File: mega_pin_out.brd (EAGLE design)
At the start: 100 x 80 mm, 11 parts, among them X1 332-36

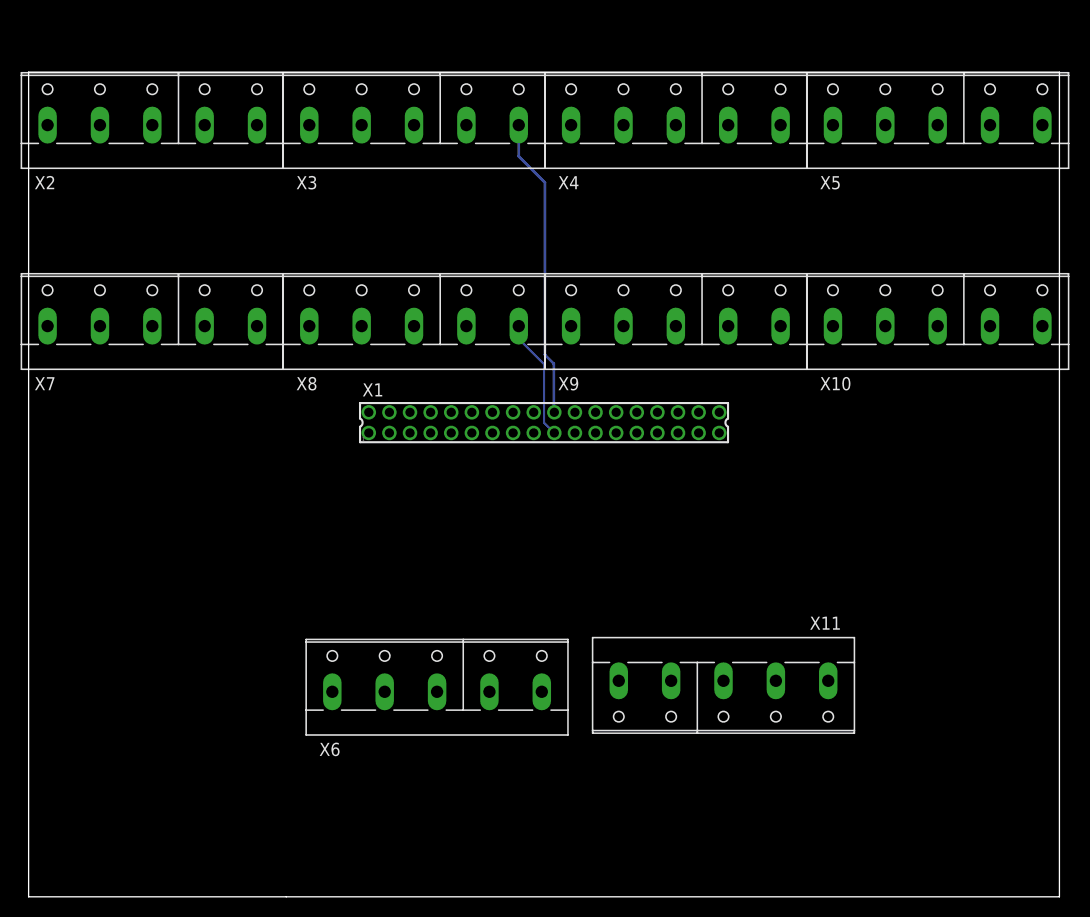
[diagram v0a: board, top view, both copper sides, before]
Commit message: Full reroute of 2x18 female pins
- Fixed the female pins pcb layout part size
- Reroute all pins
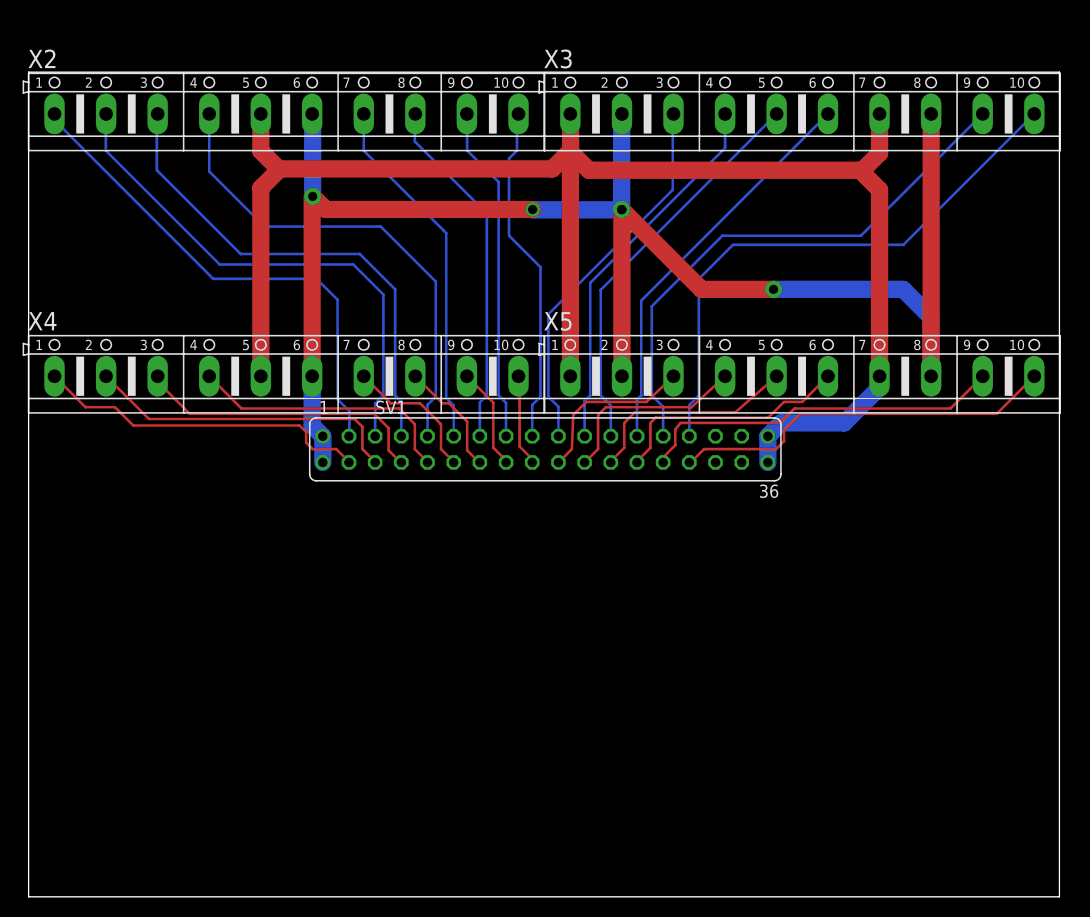
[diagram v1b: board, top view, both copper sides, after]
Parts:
- removed X1: 332-36, con-garry:332-36
- removed X10, X11, X6, X7, X8, X9: (no value), con-wago-508:W237-5P
- added SV1: (no value), con-lsta:FE18-2
- X2, X3, X4, X5: device con-wago-508:W237-5P -> con-ptr500:AK500/10
- moved X4 45.3 mm to (25.0, 50.5)
- moved X3 37.7 mm to (75.1, 75.9)
- moved X5 28.2 mm to (75.1, 50.5)
- moved X2 13.0 mm to (25.0, 75.9)
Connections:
- removed net I22: X1.3
- removed net I23: X1.4
- removed net I24: X1.5
- removed net I25: X1.6
- removed net I26: X1.7
- removed net I27: X1.8
- removed net I28: X1.9
- removed net I29: X1.10
- removed net I30: X1.11
- removed net I32: X1.13
- removed net I34: X1.15
- removed net I36: X1.17
- removed net I37: X1.18
- removed net I38: X1.19, X8.5
- removed net I39: X1.20, X3.5
- removed net N$1: X3.1
- removed net N$2: X3.2
- removed net N$30: X1.24
- removed net N$31: X1.26
- removed net N$32: X1.28
- removed net N$33: X1.30
- removed net N$34: X1.32
- removed net N$35: X1.34
- removed net N$36: X1.36
- removed net N$37: X6.1
- removed net N$38: X6.2
- removed net N$39: X6.3
- removed net N$40: X6.4
- removed net N$41: X6.5
- removed net N$42: X8.4
- removed net N$43: X8.3
- removed net N$6: X2.1
- removed net N$7: X2.2
- removed net N$8: X2.3
- new net GND: SV1.35, SV1.36, X2.5, X3.1, X3.7, X4.5, X5.1, X5.7
- new net I47: SV1.27, X3.9
- new net I49: SV1.29, X3.10
- net 5V: now also SV1.1, SV1.2, X2.6, X3.2, X3.8, X4.6, X5.2, X5.8; no longer X1.1, X1.2
- net I31: now also SV1.11, X2.7; no longer X1.12
- net I33: now also SV1.13, X2.8; no longer X1.14
- net I35: now also SV1.15, X2.9; no longer X1.16
- net N$10: now also SV1.9, X2.4; no longer X2.5
- net N$11: now also SV1.17, X2.10; no longer X1.21
- net N$12: now also SV1.19, X3.3; no longer X1.23
- net N$13: now also SV1.21, X3.4; no longer X1.25
- net N$14: now also SV1.23, X3.5; no longer X1.27
- net N$15: now also SV1.25, X3.6; no longer X1.29
- net N$16: now also SV1.4, X4.1; no longer X1.31
- net N$17: now also SV1.6, X4.2; no longer X1.33
- net N$18: now also SV1.8, X4.3; no longer X1.35
- net N$19: now also SV1.10, X4.4; no longer X4.1
- net N$20: now also SV1.12, X4.7; no longer X4.2
- net N$21: now also SV1.14, X4.8; no longer X4.3
- net N$22: now also SV1.16, X4.9; no longer X4.4
- net N$23: now also SV1.18, X4.10; no longer X4.5
- net N$24: now also SV1.20, X5.3; no longer X5.1
- net N$25: now also SV1.22, X5.4; no longer X5.2
- net N$26: now also SV1.24, X5.5; no longer X5.3
- net N$27: now also SV1.26, X5.6; no longer X5.4
- net N$28: now also SV1.28, X5.9; no longer X5.5
- net N$29: now also SV1.30, X5.10; no longer X1.22
- net N$3: now also SV1.3, X2.1; no longer X3.3
- net N$4: now also SV1.5, X2.2; no longer X3.4
- net N$9: now also SV1.7, X2.3; no longer X2.4
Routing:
- net GND: track 0.00 -> 157.4 mm
- net 5V: track 0.00 -> 155.8 mm, vias 0 -> 5
- net I49: track 0.00 -> 54.8 mm
- net I47: track 0.00 -> 52.9 mm
- net N$4: track 0.00 -> 50.3 mm
- net N$3: track 0.00 -> 49.0 mm
- net N$9: track 0.00 -> 47.9 mm
- net N$10: track 0.00 -> 47.3 mm
- net N$15: track 0.00 -> 38.9 mm
- net N$14: track 0.00 -> 38.7 mm
- net N$29: track 0.00 -> 37.5 mm
- net N$13: track 0.00 -> 37.0 mm
- net N$12: track 0.00 -> 36.7 mm
- net N$28: track 0.00 -> 35.7 mm
- net I31: track 0.00 -> 34.9 mm
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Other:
- outline, holes or cut-outs redrawn

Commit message: [BACK] Added capacitors for PIN 39 & 40 and others
* Schematic:
- Added text field for pin numbers name
- Added charging capacitors for pin 39 & 40 which are used as AC light state detectors. 

* Board
- Increased board layout from 100x80 to 100x85
- Increased clearance between terminal blocks to ~22.86 mm which was tested on breadboard to be easier during wiring. 
- Routed the capacitors
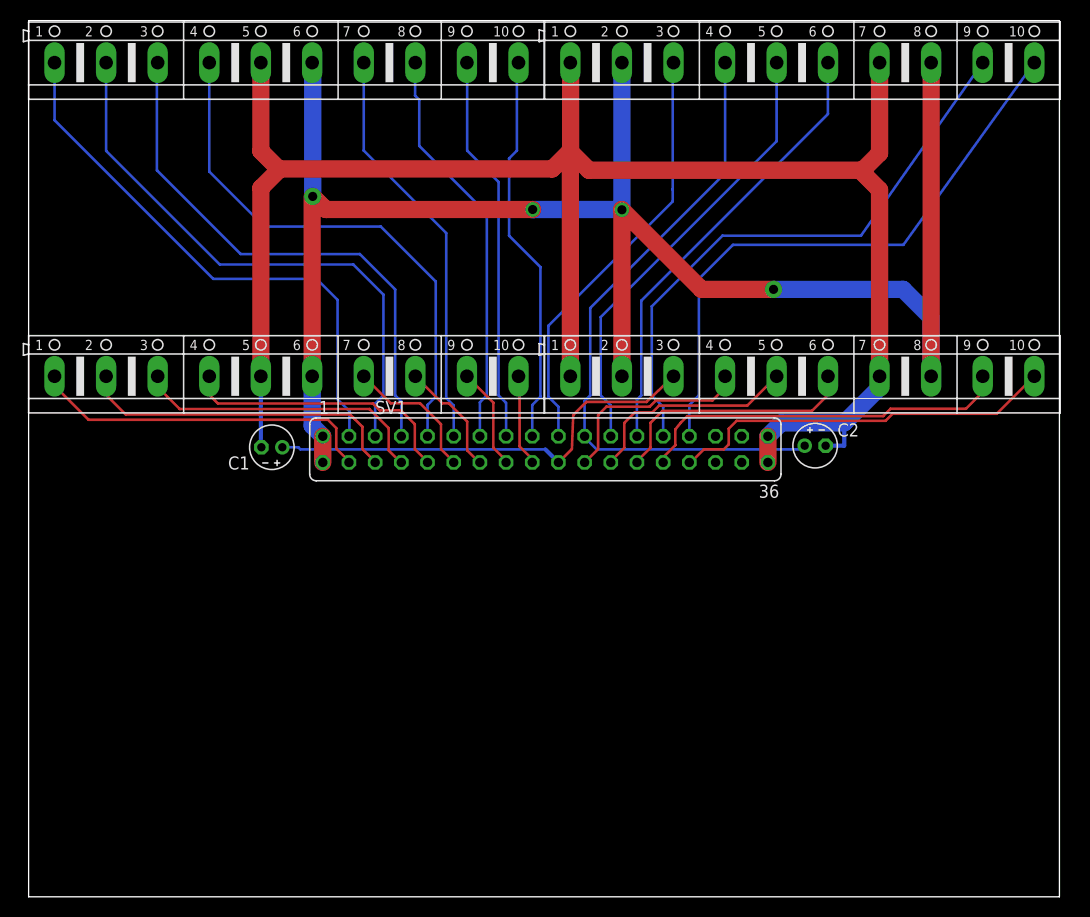
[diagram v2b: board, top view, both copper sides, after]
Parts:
- added C1, C2: 1uF, adafruit:E2-4
- moved X2 4.98 mm to (25.0, 80.9)
- moved X3 4.98 mm to (75.1, 80.9)
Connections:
- net GND: now also C1.-, C2.-
- net N$13: now also C2.+
- net N$24: now also C1.+
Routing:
- net GND: track 157.4 -> 188.3 mm
- net N$24: track 16.4 -> 43.8 mm
- net N$13: track 37.0 -> 64.1 mm
- net 5V: track 155.8 -> 170.8 mm, vias 5 -> 4
- net I33: track 34.5 -> 39.5 mm
- net N$4: track 50.3 -> 55.3 mm
- net N$15: track 38.9 -> 43.9 mm
- net N$14: track 38.7 -> 43.7 mm
- net N$12: track 36.7 -> 41.7 mm
- net N$10: track 47.3 -> 52.3 mm
- net I35: track 32.8 -> 37.8 mm
- net I31: track 34.9 -> 39.9 mm
- net N$3: track 49.0 -> 54.0 mm
- net N$11: track 33.3 -> 38.3 mm
- net N$9: track 47.9 -> 52.9 mm
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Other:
- board size 100 x 80 mm -> 100 x 85 mm

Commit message: [BUG][MAJOR] Fix wrong orientation of pin header
- Pin header connections were all wrong and mirrored. To fix it, I mirrored the header in schematics and rerouted the wrong pins.
- Added labels
- increased the distance between the two terminal block rows to ~31 cm
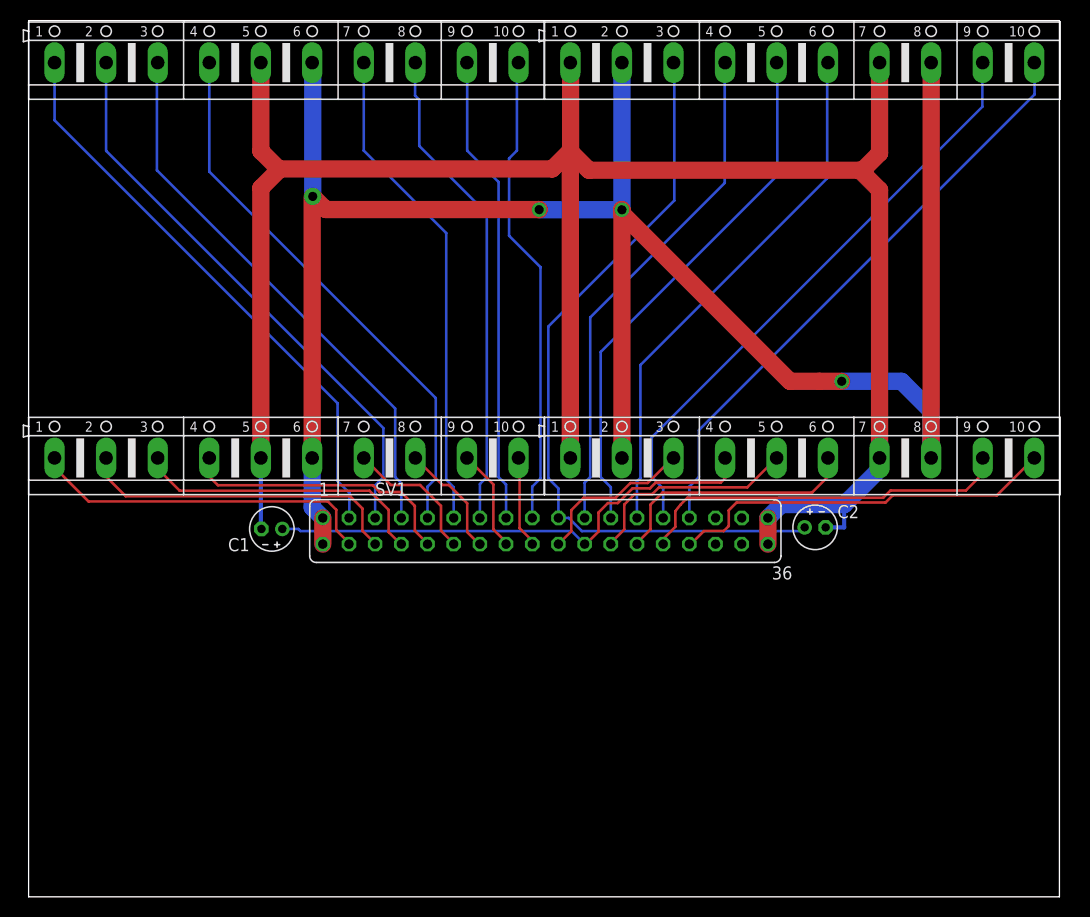
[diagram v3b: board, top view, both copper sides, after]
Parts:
- moved C1 7.92 mm to (23.6, 35.7)
- moved C2 7.92 mm to (76.3, 35.8)
- moved SV1 7.92 mm to (50.1, 35.5)
- moved X4 7.92 mm to (25.0, 42.6)
- moved X5 7.92 mm to (75.1, 42.6)
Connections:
- removed net N$12: SV1.19, X3.3
- removed net N$25: SV1.22, X5.4
- new net N$1: C2.+, SV1.19, X3.3
- new net N$2: SV1.20, X5.3
- net N$13: no longer C2.+
- net N$24: now also SV1.22, X5.4; no longer SV1.20, X5.3
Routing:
- net N$1: track 0.00 -> 74.2 mm
- net N$12: track 41.7 -> 0.00 mm
- net 5V: track 170.8 -> 197.3 mm
- net GND: track 188.3 -> 212.1 mm
- net N$25: track 19.7 -> 0.00 mm
- net N$2: track 0.00 -> 15.8 mm
- net N$13: track 64.1 -> 49.9 mm
- net N$14: track 43.7 -> 53.3 mm
- net N$11: track 38.3 -> 46.2 mm
- net N$15: track 43.9 -> 51.8 mm
- net I35: track 37.8 -> 45.7 mm
- net I33: track 39.5 -> 47.4 mm
- net I31: track 39.9 -> 47.8 mm
- net N$24: track 43.8 -> 49.3 mm
- net N$3: track 54.0 -> 56.0 mm
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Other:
- board text added: "22 24 26 28 G 5V 30 32 34 36 G 5V 38 40 42 44 G 5V 46 48"
- board text added: "23 25 27 29 G 5V 31 33 35 37 G 5V 39 41 43 45 G 5V 47 49"
- board text added: "Light"
- board text added: "PA-"
- board text added: "PC-"
- board text added: "PL-"
